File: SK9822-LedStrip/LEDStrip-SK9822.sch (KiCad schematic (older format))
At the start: 64 parts, among them J1 TE_1-1123723-4, J2 TE_1-1123723-4

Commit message: Connecting pads on SK9822 and changing edge cut to better hold footprints
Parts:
- removed D1, D10, D11, D12, D13, D14, D15, D16, D17, D18, D19, D2, D20, D21, D22, D23, D24, D25, D26, D27, D28, D29, D3, D30, D31, D32, D33, D34, D35, D36, D37, D38, D39, D4, D40, D41, D42, D43, D44, D45, D46, D47, D48, D49, D5, D50, D51, D52, D53, D54, D55, D56, D57, D58, D59, D6, D60, D7, D8, D9: APA102-2020, LED_SMD:LED-APA102-2020, symbol LED:APA102-2020
- added D1, D10, D11, D12, D13, D14, D15, D16, D17, D18, D19, D2, D20, D21, D22, D23, D24, D25, D26, D27, D28, D29, D3, D30, D31, D32, D33, D34, D35, D36, D37, D38, D39, D4, D40, D5, D6, D7, D8, D9: SK9822, SK9822:SK9822, symbol sk9822:SK9822
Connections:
- wire segments 160 -> 110

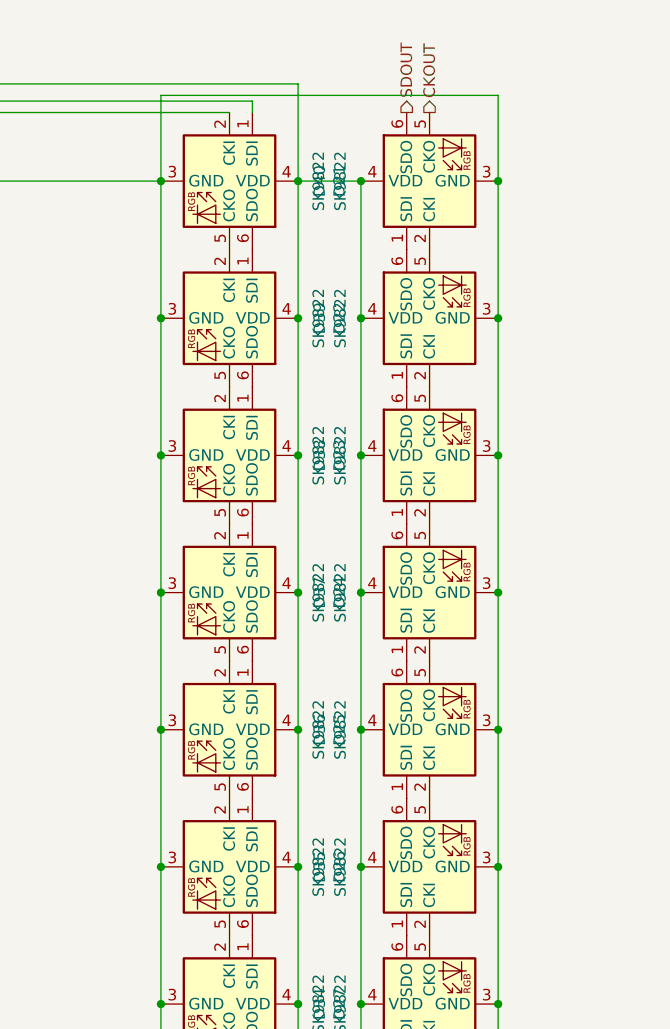
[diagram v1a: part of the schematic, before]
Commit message: Adding Depot 37 logo and removing wings from the middle of sk9822 pcb
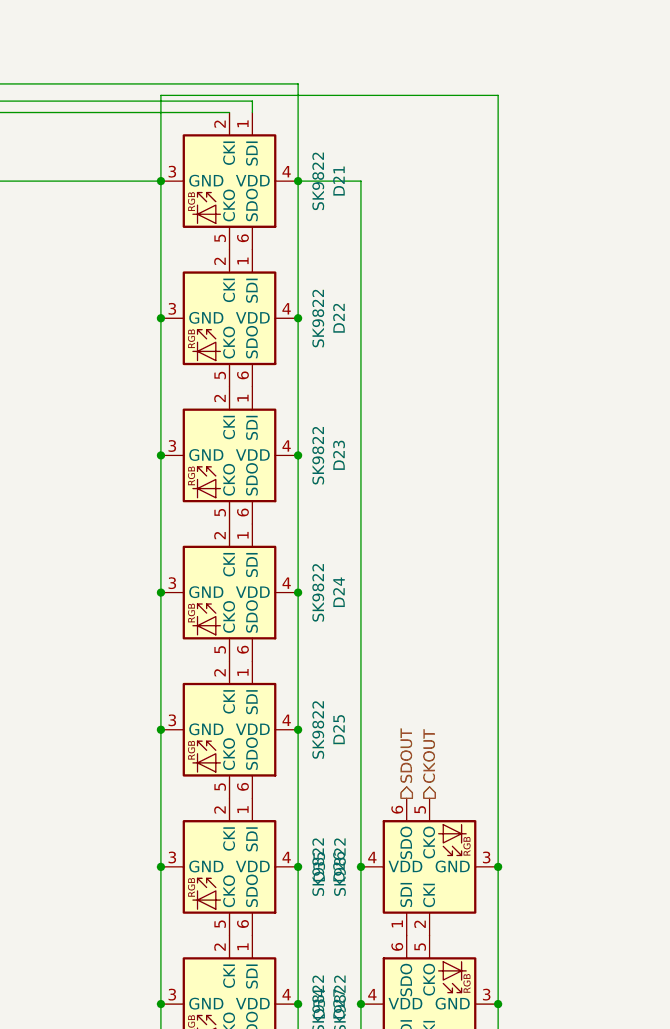
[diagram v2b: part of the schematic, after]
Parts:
- removed D36, D37, D38, D39, D40: SK9822, SK9822:SK9822, symbol sk9822:SK9822
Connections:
- net CKOUT: now also D35.5 (CKO)
- net SDOUT: now also D35.6 (SDO)
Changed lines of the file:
@@
 Text HLabel 2875 7350 1    50   Input ~ 0
 VDD
-Text HLabel 5250 925  1    50   Output ~ 0
+Text HLabel 5250 3925 1    50   Output ~ 0
 CKOUT
-Text HLabel 5150 925  1    50   Output ~ 0
+Text HLabel 5150 3925 1    50   Output ~ 0
 SDOUT
 $Comp
@@
 	0    1    1    0
 $EndComp
-Wire Wire Line
-	4950 1225 4950 1825
-Wire Wire Line
-	5550 850  5550 1225
 $Comp
 L sk9822:SK9822 D31
@@
 Wire Wire Line
 	4950 4225 4950 4825
-$Comp
-L sk9822:SK9822 D36
-U 1 1 61AC2A87
-P 5250 3625
-F 0 "D36" H 5250 4106 50  0000 C CNN
-F 1 "SK9822" H 5250 4015 50  0000 C CNN
-F 2 "SK9822:SK9822" H 5300 3325 50  0001 L TNN
-F 3 "https://cdn-shop.adafruit.com/product-files/2351/SK9822_datasheet_SHIJI.pdf" H 5350 3250 50  0001 L TNN
-	1    5250 3625
-	0    -1   -1   0
-$EndComp
-Connection ~ 5550 3625
-Wire Wire Line
-	5550 3625 5550 4225
-Connection ~ 4950 3625
-Wire Wire Line
-	4950 3625 4950 4225
-$Comp
-L sk9822:SK9822 D37
-U 1 1 61AC3233
-P 5250 3025
-F 0 "D37" H 5250 3506 50  0000 C CNN
-F 1 "SK9822" H 5250 3415 50  0000 C CNN
-F 2 "SK9822:SK9822" H 5300 2725 50  0001 L TNN
-F 3 "https://cdn-shop.adafruit.com/product-files/2351/SK9822_datasheet_SHIJI.pdf" H 5350 2650 50  0001 L TNN
-	1    5250 3025
-	0    -1   -1   0
-$EndComp
-Connection ~ 5550 3025
-Wire Wire Line
-	5550 3025 5550 3625
-Connection ~ 4950 3025
-Wire Wire Line
-	4950 3025 4950 3625
-$Comp
-L sk9822:SK9822 D38
-U 1 1 61AC3ABD
-P 5250 2425
-F 0 "D38" H 5250 2906 50  0000 C CNN
-F 1 "SK9822" H 5250 2815 50  0000 C CNN
-F 2 "SK9822:SK9822" H 5300 2125 50  0001 L TNN
-F 3 "https://cdn-shop.adafruit.com/product-files/2351/SK9822_datasheet_SHIJI.pdf" H 5350 2050 50  0001 L TNN
-	1    5250 2425
-	0    -1   -1   0
-$EndComp
-Connection ~ 5550 2425
-Wire Wire Line
-	5550 2425 5550 3025
-Connection ~ 4950 2425
-Wire Wire Line
-	4950 2425 4950 3025
-$Comp
-L sk9822:SK9822 D39
-U 1 1 61AC42A1
-P 5250 1825
-F 0 "D39" H 5250 2306 50  0000 C CNN
-F 1 "SK9822" H 5250 2215 50  0000 C CNN
-F 2 "SK9822:SK9822" H 5300 1525 50  0001 L TNN
-F 3 "https://cdn-shop.adafruit.com/product-files/2351/SK9822_datasheet_SHIJI.pdf" H 5350 1450 50  0001 L TNN
-	1    5250 1825
-	0    -1   -1   0
-$EndComp
-Connection ~ 5550 1825
-Wire Wire Line
-	5550 1825 5550 2425
-Connection ~ 4950 1825
-Wire Wire Line
-	4950 1825 4950 2425
-$Comp
-L sk9822:SK9822 D40
-U 1 1 61AC489A
-P 5250 1225
-F 0 "D40" H 5250 1706 50  0000 C CNN
-F 1 "SK9822" H 5250 1615 50  0000 C CNN
-F 2 "SK9822:SK9822" H 5300 925 50  0001 L TNN
-F 3 "https://cdn-shop.adafruit.com/product-files/2351/SK9822_datasheet_SHIJI.pdf" H 5350 850 50  0001 L TNN
-	1    5250 1225
-	0    -1   -1   0
-$EndComp
-Connection ~ 5550 1225
-Wire Wire Line
-	5550 1225 5550 1825
-Connection ~ 4950 1225
+Wire Wire Line
+	4950 1225 4950 4225
+Wire Wire Line
+	5550 850  5550 4225
 $EndSCHEMATC

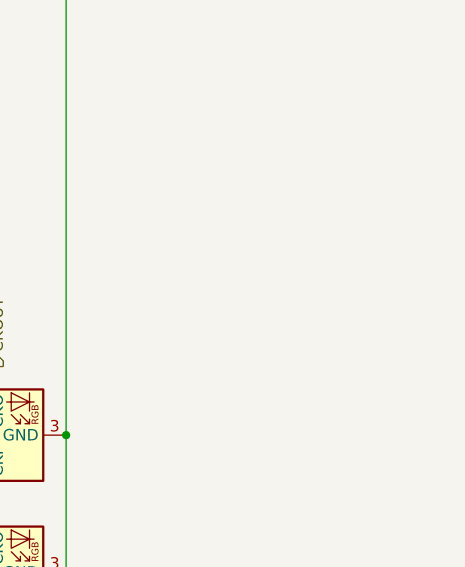
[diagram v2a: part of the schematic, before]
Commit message: Create new schematic for logic board
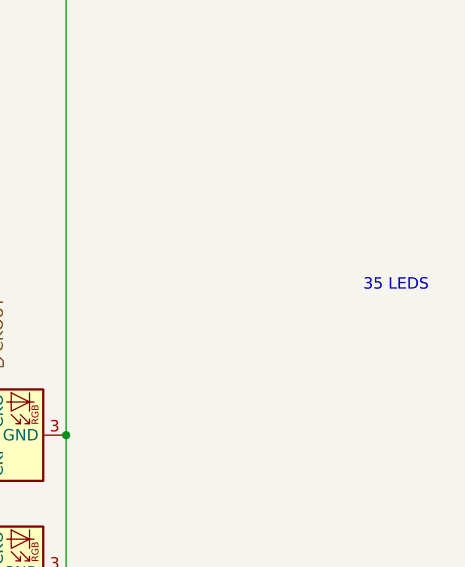
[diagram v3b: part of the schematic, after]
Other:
- note added: "35 LEDS"
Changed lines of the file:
@@
 Wire Wire Line
 	5550 850  5550 4225
+Text Notes 6850 3600 0    50   ~ 0
+35 LEDS
 $EndSCHEMATC
